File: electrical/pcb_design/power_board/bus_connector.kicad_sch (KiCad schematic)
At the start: 10 parts, among them J1 TE_Connectivity_7-5530843-7, J2 TE_Connectivity_7-5530843-7, J3 TE_Connectivity_7-5530843-7, J4 TE_Connectivity_7-5530843-7, J5 TE_Connectivity_7-5530843-7, J6 TE_Connectivity_7-5530843-7, J7 TE_Connectivity_7-5530843-7, J8 TE_Connectivity_7-5530843-7

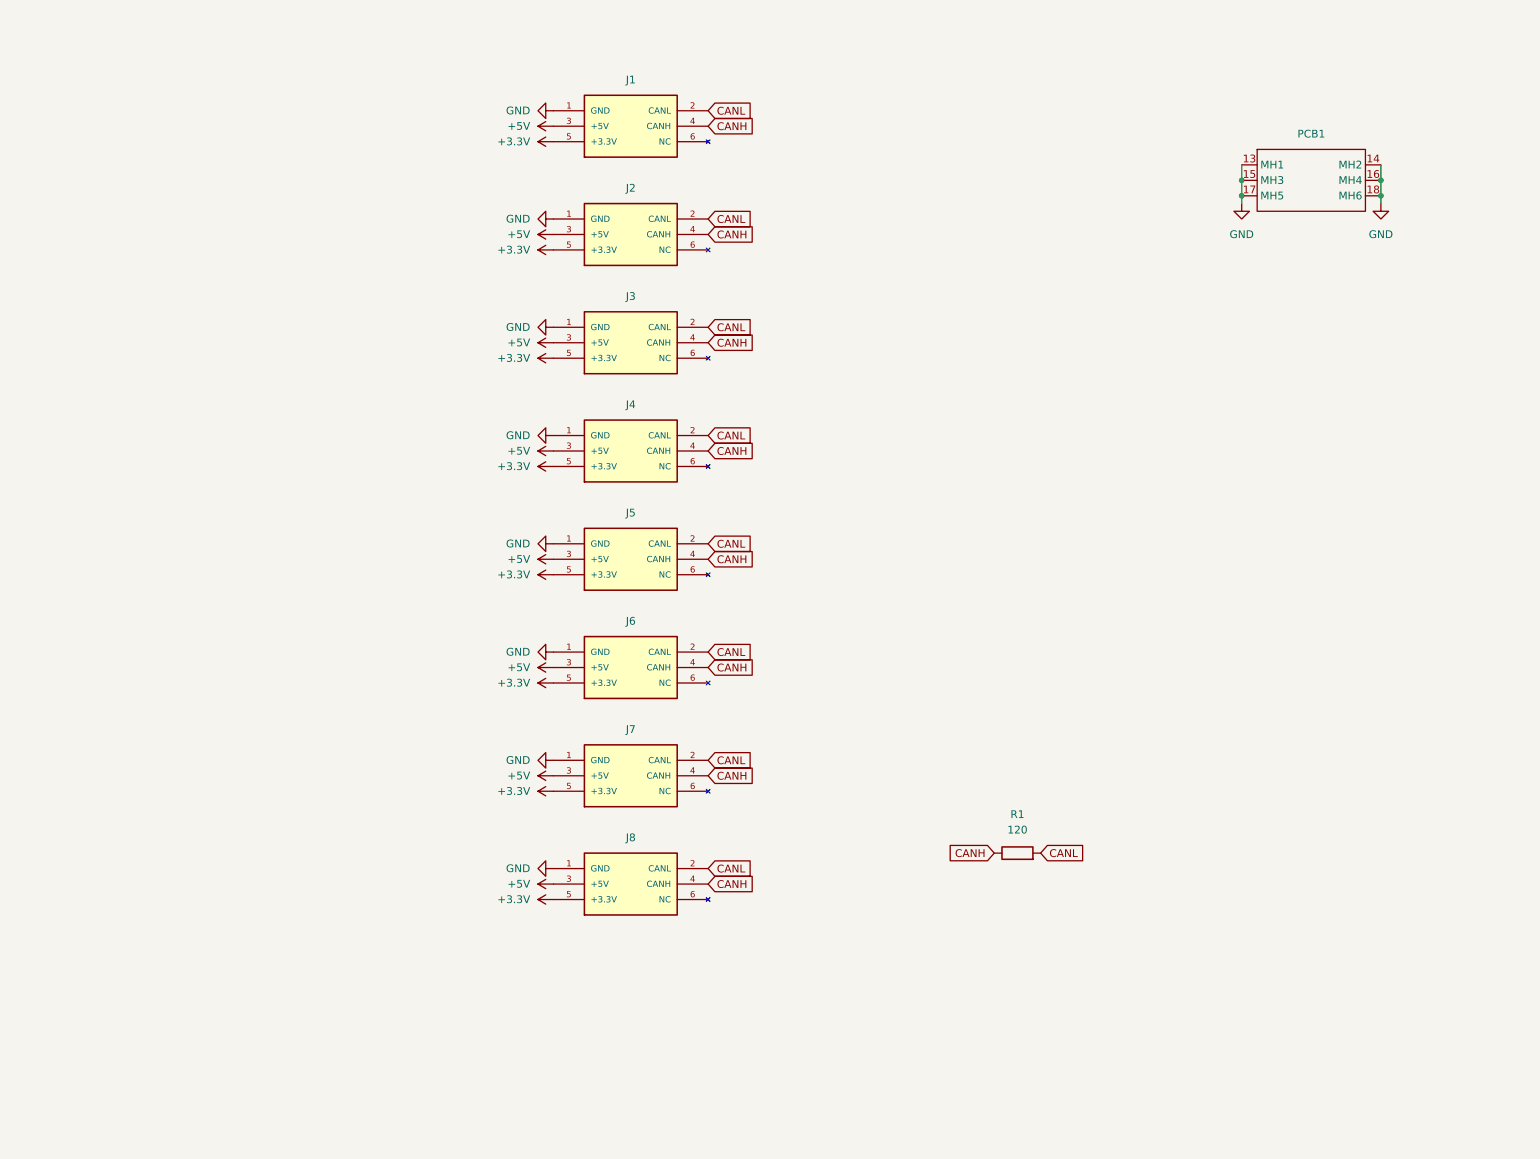
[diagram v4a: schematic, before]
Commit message: Major rework of power board for brash bakery iteration
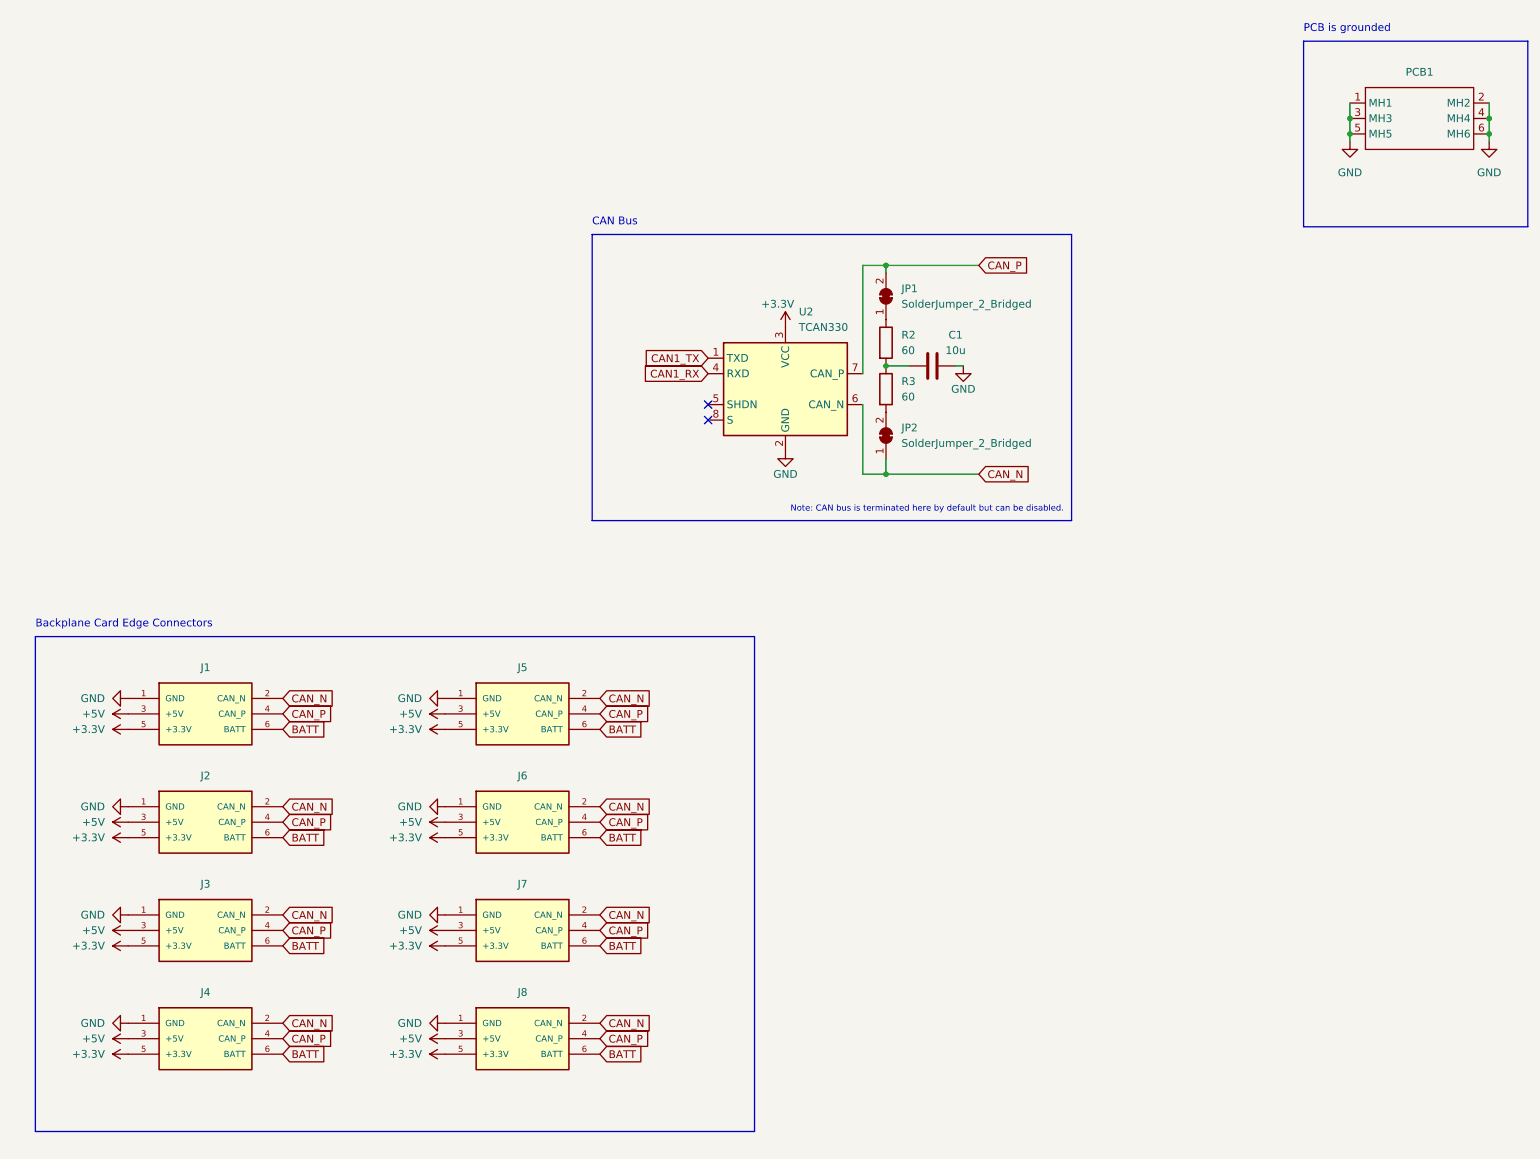
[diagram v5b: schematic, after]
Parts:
- removed R1: 120, symbol Device:R
- added C1: 10u, Capacitor_SMD:C_0603_1608Metric, symbol Device:C
- added JP1, JP2: SolderJumper_2_Bridged, Jumper:SolderJumper-2_P1.3mm_Bridged_RoundedPad1.0x1.5mm, symbol Jumper:SolderJumper_2_Bridged
- added R2, R3: 60, Resistor_SMD:R_0402_1005Metric, symbol Device:R
- added U2: TCAN330, Package_TO_SOT_SMD:SOT-23-8, symbol Interface_CAN_LIN:TCAN330
- J1, J2, J3, J4, J5, J6, J7, J8: symbol TVSC:Backplane_Connector_Reversed -> TVSC:Backplane_Connector_Producer; MPN (none) -> C4570400; Manufacturer Part Number (none) -> 7-5530843-7
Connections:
- net +3.3V: now also U2.3 (VCC)
- net GND: now also PCB1.1 (MH1), PCB1.2 (MH2), PCB1.3 (MH3), PCB1.4 (MH4), PCB1.5 (MH5), PCB1.6 (MH6), C1.2, U2.2 (GND); no longer PCB1.13 (MH1), PCB1.14 (MH2), PCB1.15 (MH3), PCB1.16 (MH4), PCB1.17 (MH5), PCB1.18 (MH6)
- net BATT: now reaches J6.6 (BATT)
- net BATT: now also J1.6 (BATT), J2.6 (BATT), J3.6 (BATT), J4.6 (BATT), J5.6 (BATT), J7.6 (BATT), J8.6 (BATT)
- net CANH renamed CAN_P
- net CAN_P: now also JP1.2 (B), U2.7 (CAN_P)
- net CANL renamed CAN_N
- net CAN_N: now also JP2.1 (A), U2.6 (CAN_N)
- new net: C1.1, R2.2, R3.1
- new net: JP2.2 (B), R3.2
- new net: JP1.1 (A), R2.1
- new net CAN1_RX: U2.4 (RXD)
- new net CAN1_TX: U2.1 (TXD)
- no-connect marks 0 -> 2
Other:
- note added: "Backplane Card Edge Connectors"
- note added: "CAN Bus"
- note added: "Note: CAN bus is terminated here by default but can be disabled."
- note added: "PCB is grounded"
- moved on the sheet: PCB1

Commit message: Checkpointing work on power board. This work includes changing out the MCU from a BGA package to one that is more easily manufactured.
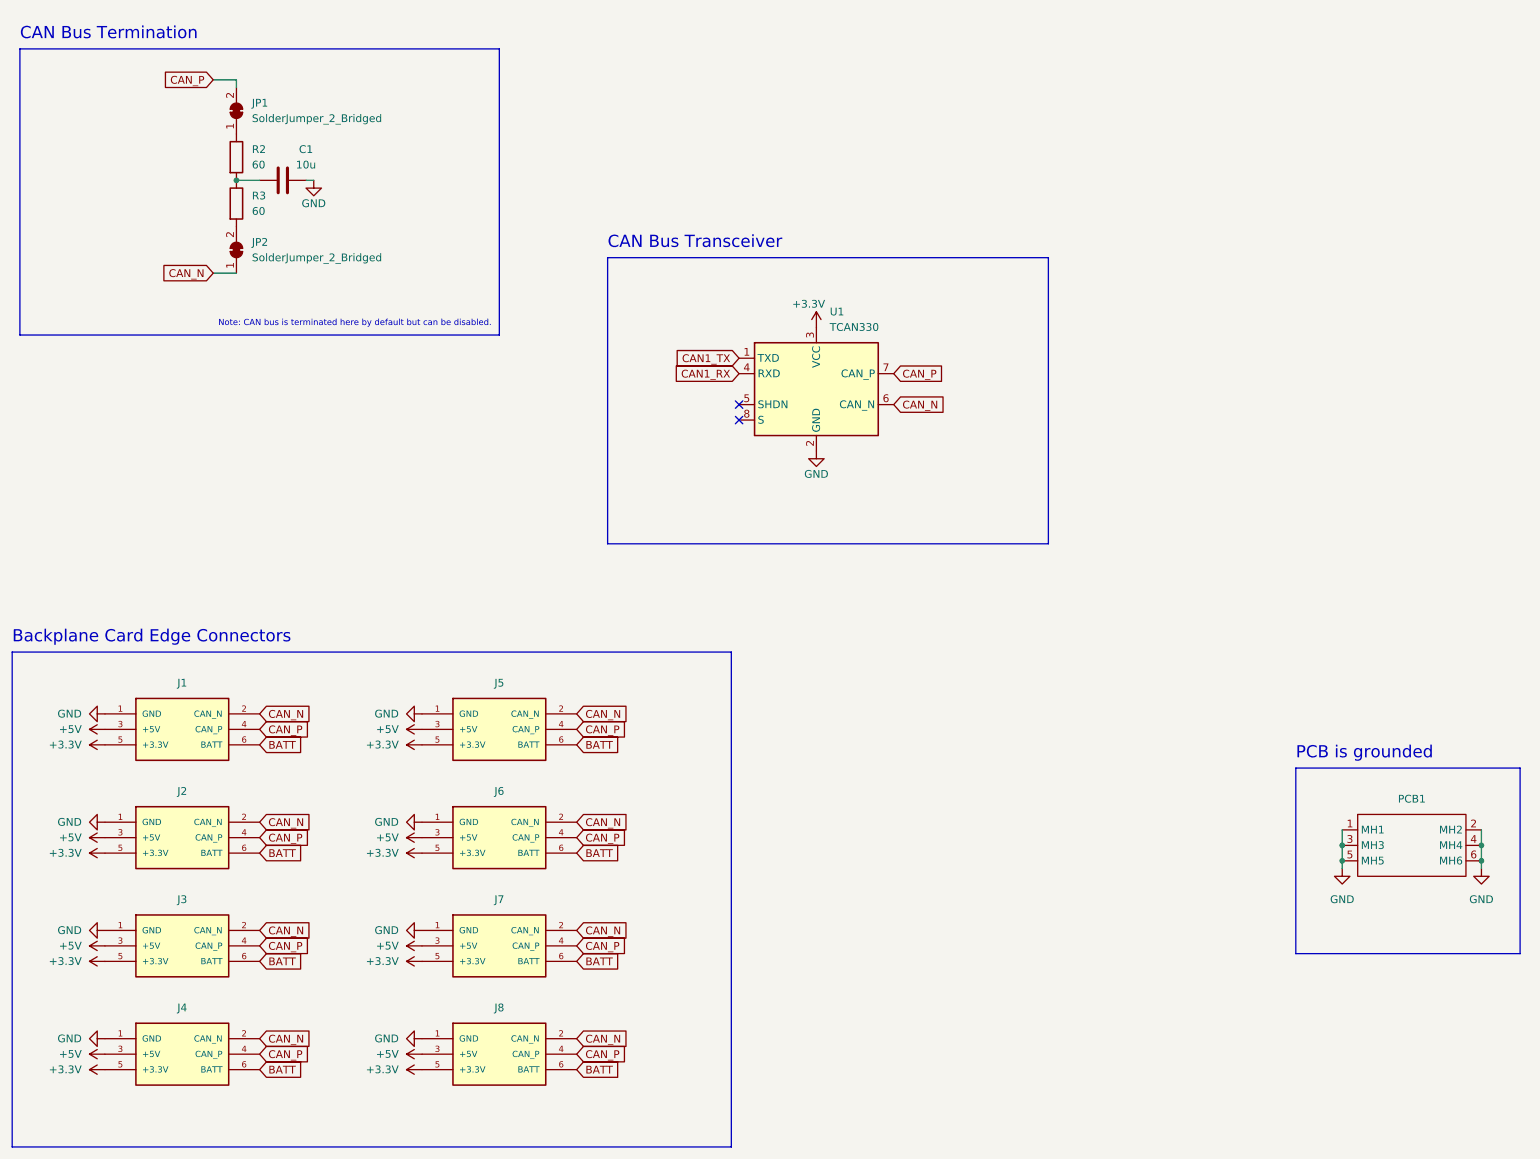
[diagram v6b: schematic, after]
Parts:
- removed U2: TCAN330, Package_TO_SOT_SMD:SOT-23-8, symbol Interface_CAN_LIN:TCAN330
- added U1: TCAN330, Package_TO_SOT_SMD:SOT-23-8, symbol Interface_CAN_LIN:TCAN330
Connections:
- net +3.3V: now also U1.3 (VCC)
- net CAN1_RX: now also U1.4 (RXD)
- net CAN1_TX: now also U1.1 (TXD)
- net CAN_N: now also U1.6 (CAN_N)
- net CAN_P: now also U1.7 (CAN_P)
- net GND: now also U1.2 (GND)
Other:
- note added: "CAN Bus Termination"
- note added: "CAN Bus Transceiver"
- note removed: "CAN Bus"
- moved on the sheet: J1, J2, J3, J4, J5, J6, J7, J8, PCB1

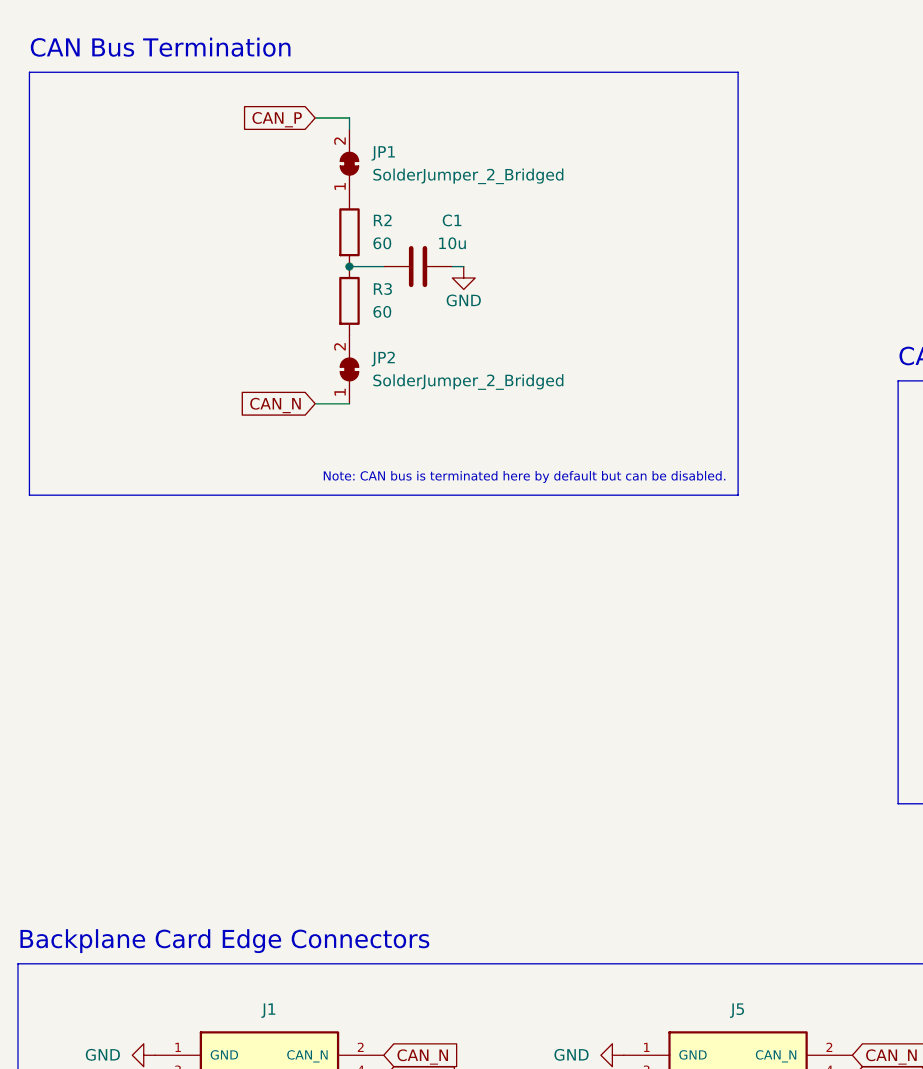
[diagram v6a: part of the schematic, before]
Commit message: Added 2nd CAN bus termination to allow this board to be self-contained. This gives us termination on both ends of the transmission line, but both can be enabled or disabled via jumpers.
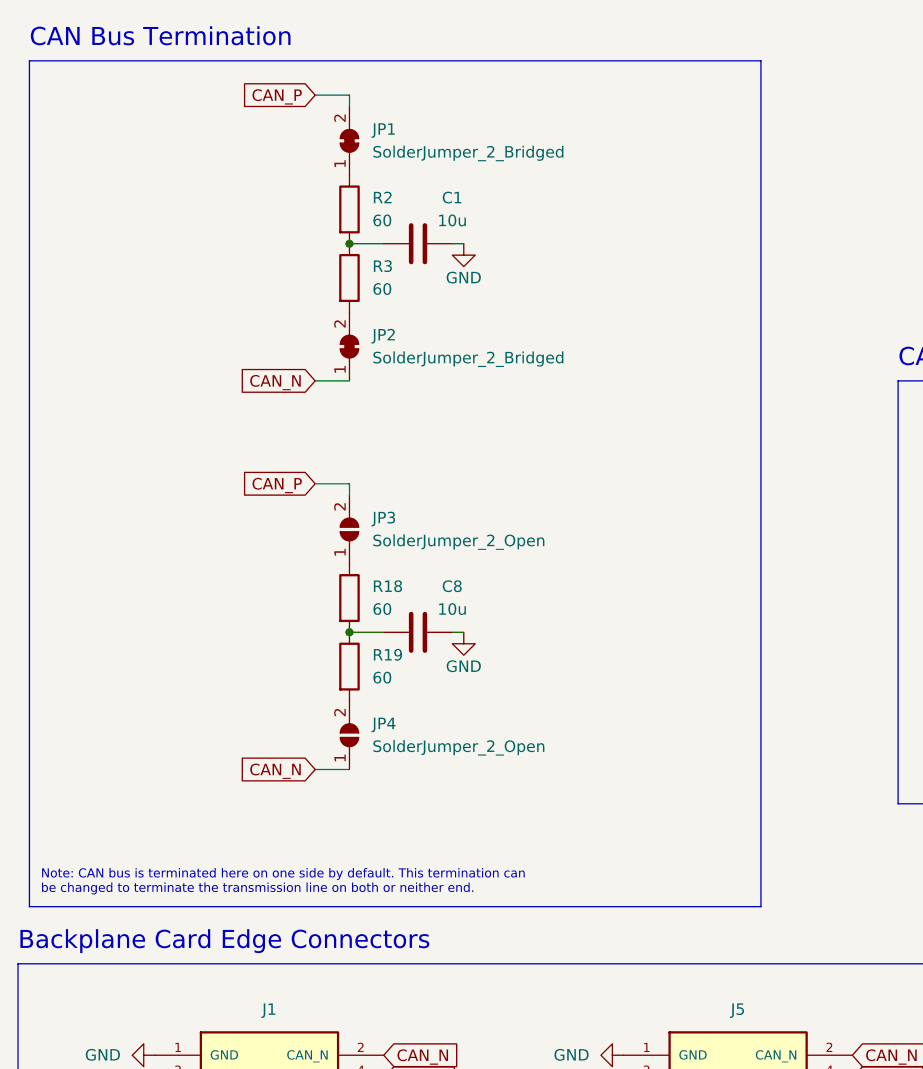
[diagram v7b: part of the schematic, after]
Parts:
- added C8: 10u, Capacitor_SMD:C_0603_1608Metric, symbol Device:C
- added JP3, JP4: SolderJumper_2_Open, Jumper:SolderJumper-2_P1.3mm_Open_RoundedPad1.0x1.5mm, symbol Jumper:SolderJumper_2_Open
- added R18, R19: 60, Resistor_SMD:R_0402_1005Metric, symbol Device:R
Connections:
- net CAN_N: now also JP4.1 (A)
- net CAN_P: now also JP3.2 (B)
- net GND: now also C8.2
- new net: JP4.2 (B), R19.2
- new net: C8.1, R18.2, R19.1
- new net: JP3.1 (A), R18.1
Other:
- note added: "Note: CAN bus is terminated here on one side by default. This termination can be changed to terminate the transmission line on both or neither end."
- note removed: "Note: CAN bus is terminated here by default but can be disabled."
- moved on the sheet: C1, JP1, JP2, R2, R3
